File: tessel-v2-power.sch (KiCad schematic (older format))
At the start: 54 parts, among them Q301 MMSS8550, U301 AAT4610, U302 AAT4610, U303 AP3417C, U304 AP3417C, U305 AP3418

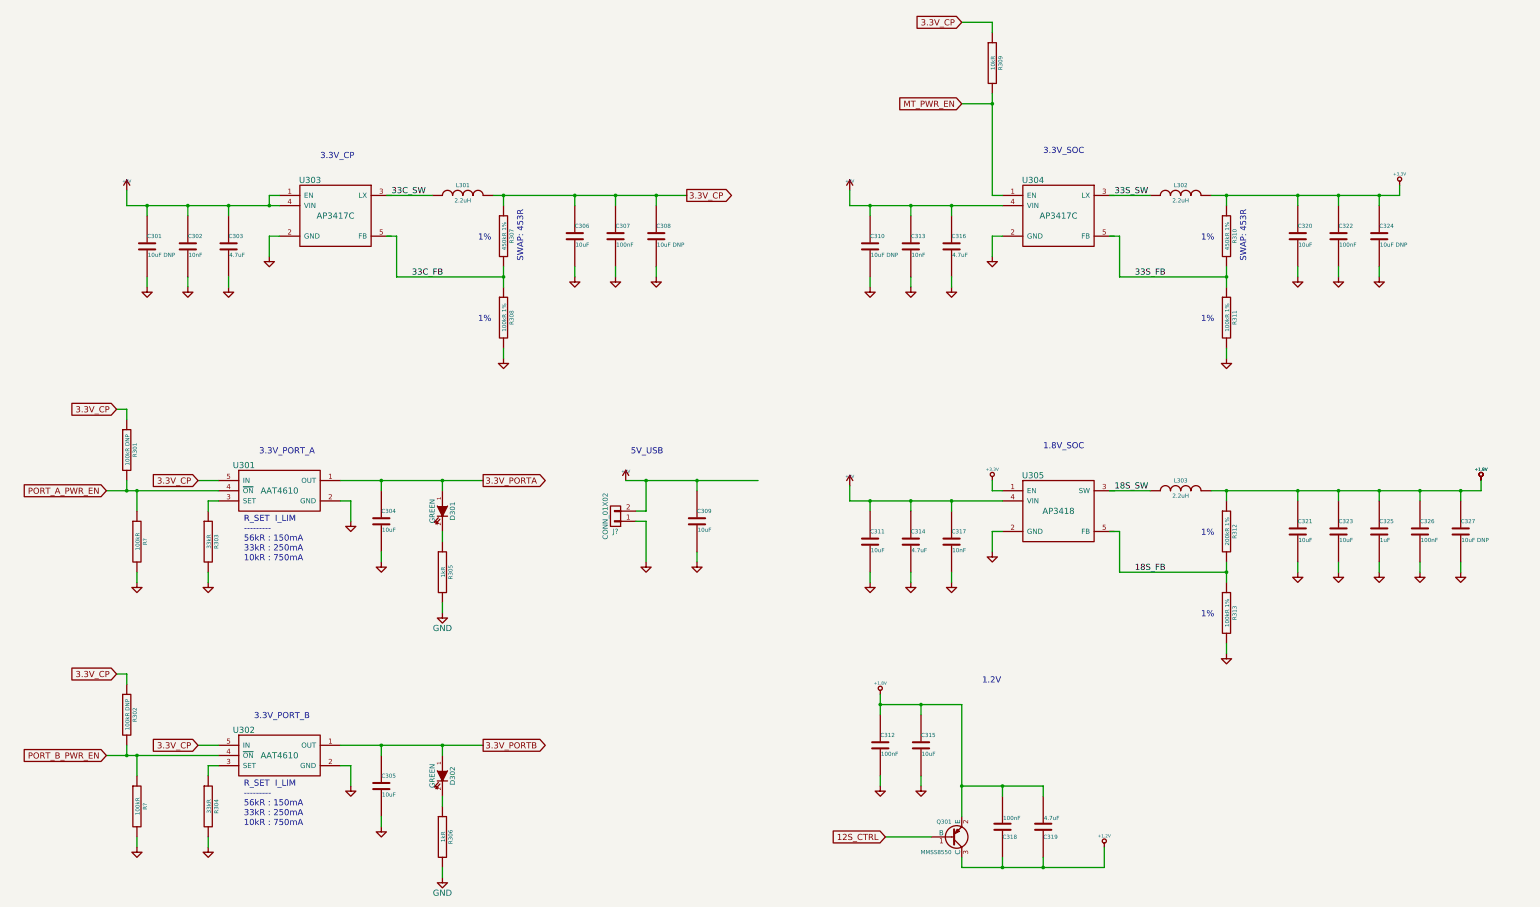
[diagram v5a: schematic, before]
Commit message: added testpoints to swd and power
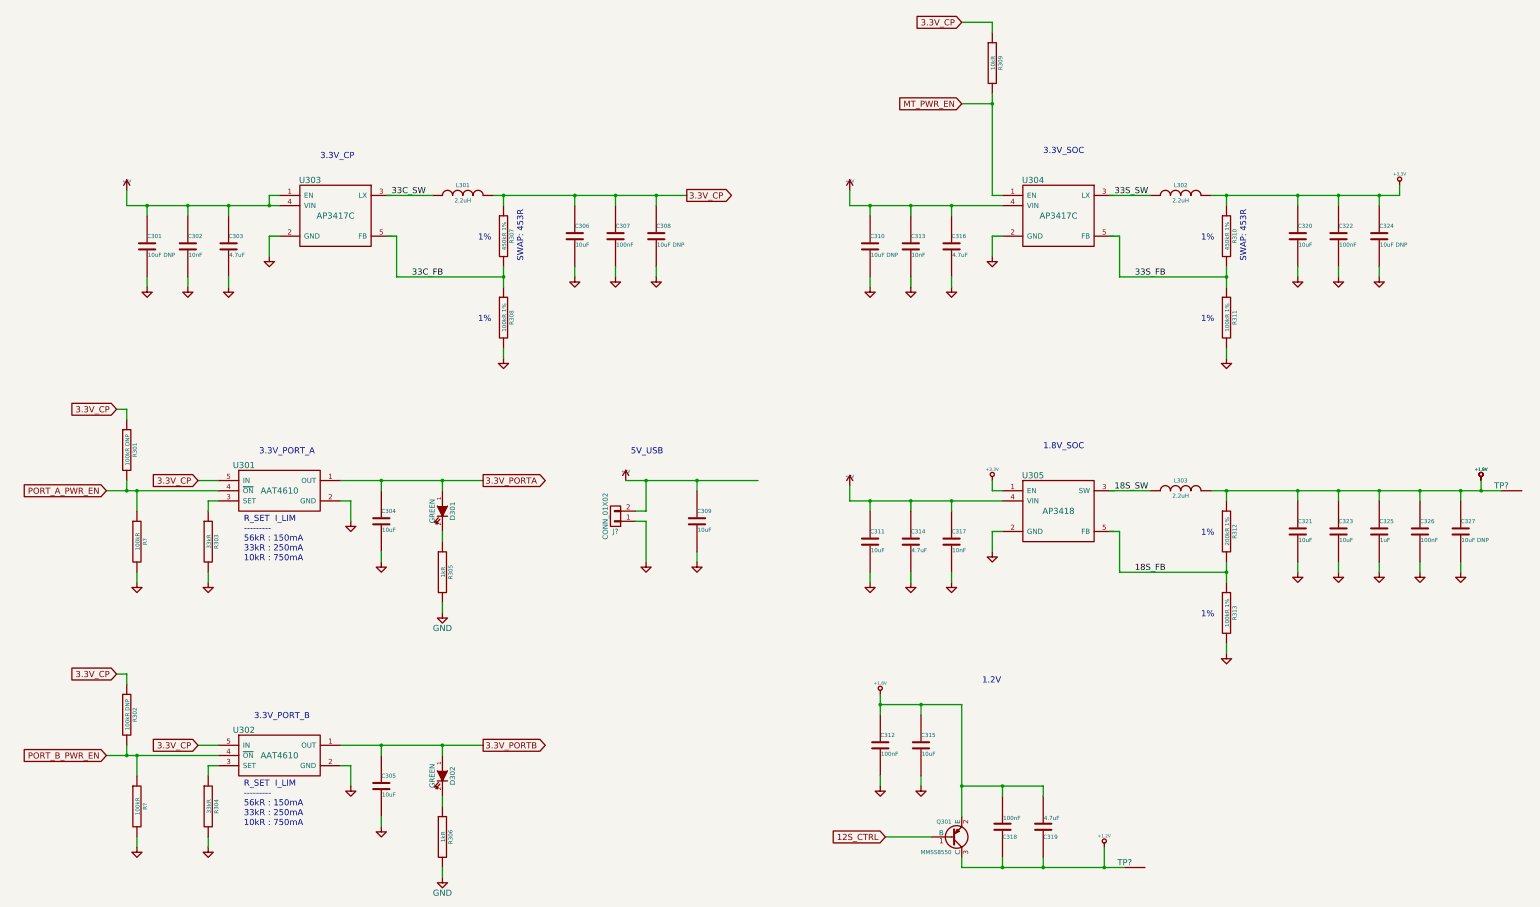
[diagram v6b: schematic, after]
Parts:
- added TP? (x2): TP, symbol TP
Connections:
- wire segments 189 -> 145
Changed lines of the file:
@@
 Connection ~ 9300 7800
 Wire Wire Line
-	9300 7700 9300 7800
-Wire Wire Line
-	9300 7800 9300 7900
+	9300 7700 9300 7900
 Wire Wire Line
 	10400 5700 10400 5600
@@
 	9600 5800 9600 5900
 Wire Wire Line
-	9000 5800 9200 5800
-Wire Wire Line
-	9200 5800 9600 5800
-Wire Wire Line
-	9600 5800 10000 5800
-Wire Wire Line
-	10000 5800 10500 5800
+	9000 5800 10500 5800
 Wire Wire Line
 	9200 5900 9200 5800
@@
 	12700 5700 12700 5800
 Wire Wire Line
-	12550 5700 12700 5700
-Wire Wire Line
-	12700 5700 13400 5700
-Wire Wire Line
-	13400 5700 13800 5700
-Wire Wire Line
-	13800 5700 14200 5700
-Wire Wire Line
-	14200 5700 14600 5700
-Wire Wire Line
-	14600 5700 15000 5700
-Wire Wire Line
-	15000 5700 15200 5700
+	12550 5700 15400 5700
 Connection ~ 12700 6500
 Wire Wire Line
-	12700 6400 12700 6500
-Wire Wire Line
-	12700 6500 12700 6600
+	12700 6400 12700 6600
 Wire Wire Line
 	14400 2800 14400 2700
@@
 Connection ~ 10400 1900
 Wire Wire Line
-	10400 1800 10400 1900
-Wire Wire Line
-	10400 1900 10400 2800
+	10400 1800 10400 2800
 Wire Wire Line
 	10100 1900 10400 1900
@@
 	9600 2900 9600 3000
 Wire Wire Line
-	9000 2900 9200 2900
-Wire Wire Line
-	9200 2900 9600 2900
-Wire Wire Line
-	9600 2900 10000 2900
-Wire Wire Line
-	10000 2900 10500 2900
+	9000 2900 10500 2900
 Wire Wire Line
 	9200 3000 9200 2900
@@
 	12700 2800 12700 2900
 Wire Wire Line
-	12550 2800 12700 2800
-Wire Wire Line
-	12700 2800 13400 2800
-Wire Wire Line
-	13400 2800 13800 2800
-Wire Wire Line
-	13800 2800 14200 2800
-Wire Wire Line
-	14200 2800 14400 2800
+	12550 2800 14400 2800
 Connection ~ 12700 3600
 Wire Wire Line
-	12700 3500 12700 3600
-Wire Wire Line
-	12700 3600 12700 3700
+	12700 3500 12700 3700
 Wire Wire Line
 	3300 3200 3300 3400
@@
 	2600 8200 2800 8200
 Wire Wire Line
-	4000 8200 4400 8200
-Wire Wire Line
-	4400 8200 5000 8200
-Wire Wire Line
-	5000 8200 5400 8200
-Wire Wire Line
-	1700 8300 1900 8300
-Wire Wire Line
-	1900 8300 2000 8300
-Wire Wire Line
-	2000 8300 2800 8300
+	4000 8200 5400 8200
+Wire Wire Line
+	1700 8300 2800 8300
 Connection ~ 4400 5600
 Wire Wire Line
@@
 	10500 8600 10500 8700
 Wire Wire Line
-	10100 8600 10500 8600
-Wire Wire Line
-	10500 8600 10900 8600
-Wire Wire Line
-	10100 9400 10500 9400
-Wire Wire Line
-	10500 9400 10900 9400
-Wire Wire Line
-	10900 9400 11500 9400
+	10100 8600 10900 8600
+Wire Wire Line
+	10100 9400 11700 9400
 Wire Wire Line
 	10500 9300 10500 9400
@@
 	4100 5800 4100 6000
 Wire Wire Line
-	9300 7800 9700 7800
-Wire Wire Line
-	9700 7800 10100 7800
-Wire Wire Line
-	10100 7800 10100 8600
-Wire Wire Line
-	10100 8600 10100 8900
+	9300 7800 10100 7800
+Wire Wire Line
+	10100 7800 10100 8900
 Wire Wire Line
 	9800 9100 9350 9100
@@
 	2600 5600 2800 5600
 Wire Wire Line
-	4000 5600 4400 5600
-Wire Wire Line
-	4400 5600 5000 5600
-Wire Wire Line
-	5000 5600 5400 5600
-Wire Wire Line
-	1700 5700 1900 5700
-Wire Wire Line
-	1900 5700 2000 5700
-Wire Wire Line
-	2000 5700 2800 5700
+	4000 5600 5400 5600
+Wire Wire Line
+	1700 5700 2800 5700
 Connection ~ 2100 2900
 Connection ~ 2500 2900
@@
 	2500 2900 2500 3000
 Wire Wire Line
-	1900 2900 2100 2900
-Wire Wire Line
-	2100 2900 2500 2900
-Wire Wire Line
-	2500 2900 2900 2900
-Wire Wire Line
-	2900 2900 3300 2900
-Wire Wire Line
-	3300 2900 3400 2900
+	1900 2900 3400 2900
 Wire Wire Line
 	2100 3000 2100 2900
@@
 	5600 2800 5600 2900
 Wire Wire Line
-	5500 2800 5600 2800
-Wire Wire Line
-	5600 2800 6300 2800
-Wire Wire Line
-	6300 2800 6700 2800
-Wire Wire Line
-	6700 2800 7100 2800
-Wire Wire Line
-	7100 2800 7400 2800
+	5500 2800 7400 2800
 Connection ~ 5600 3600
 Wire Wire Line
-	5600 3500 5600 3600
-Wire Wire Line
-	5600 3600 5600 3700
+	5600 3500 5600 3700
 Wire Wire Line
 	7500 6300 7500 6400
 Connection ~ 7500 5600
 Wire Wire Line
-	7500 5700 7500 5600
-Wire Wire Line
-	6800 5600 7000 5600
-Wire Wire Line
-	7000 5600 7500 5600
-Wire Wire Line
-	7500 5600 8100 5600
+	7500 5600 7500 5700
+Wire Wire Line
+	6800 5600 8100 5600
 Wire Wire Line
 	9300 8500 9300 8600
@@
 Wire Wire Line
 	7000 6000 7000 6400
+$Comp
+L TP TP?
+U 1 1 550782AD
+P 15400 5700
+F 0 "TP?" H 15400 5750 60  0000 C CNN
+F 1 "TP" H 15400 5650 60  0001 C CNN
+F 2 "" H 15400 5700 60  0000 C CNN
+F 3 "" H 15400 5700 60  0000 C CNN
+	1    15400 5700
+	1    0    0    -1
+$EndComp
+Connection ~ 15200 5700
+$Comp
+L TP TP?
+U 1 1 55078BE1
+P 11700 9400
+F 0 "TP?" H 11700 9450 60  0000 C CNN
+F 1 "TP" H 11700 9350 60  0001 C CNN
+F 2 "" H 11700 9400 60  0000 C CNN
+F 3 "" H 11700 9400 60  0000 C CNN
+	1    11700 9400
+	1    0    0    -1
+$EndComp
+Connection ~ 11500 9400
 $EndSCHEMATC

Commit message: annotated
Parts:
- gave numbers to parts that had none: 5

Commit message: netlist, etc.
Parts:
- J301: footprint (none) -> Pin_Headers:Pin_Header_Straight_1x02
- TP301, TP302: footprint (none) -> tm-kicad-lib:Testpoint
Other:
- moved on the sheet: C306, C307, C308, C320, C321, C322, C323, C324, C325, C326, C327, L301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
